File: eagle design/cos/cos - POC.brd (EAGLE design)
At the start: 35 x 63 mm, 105 parts, among them IC1 SQJ952EP-T1_GE3, IC10 PBRC8.00GR50X000, IC12 LM74670QDGKRQ1, IC14 MCP73871-2CCI/ML, IC15 MCP23S08-E/ML, IC16 LDK320M50R, IC17 MCP2515, IC18 LM74670QDGKRQ1, IC19 MCP2561-2, IC2 SQJ952EP-T1_GE3, IC20 AD5160BRJZ5-R2, IC21 MP3221GJ-P, IC22 SQJ952EP-T1_GE3, IC23 LM74670QDGKRQ1, IC24 LM74670QDGKRQ1, IC3 TPS630702RNMT, IC4 LM74670QDGKRQ1, IC5 SQJ952EP-T1_GE3, IC6 FDMQ8403, IC7 LMP92064SD/NOPB, IC8 ATTINY4313-MMH, IC9 LM74670QDGKRQ1

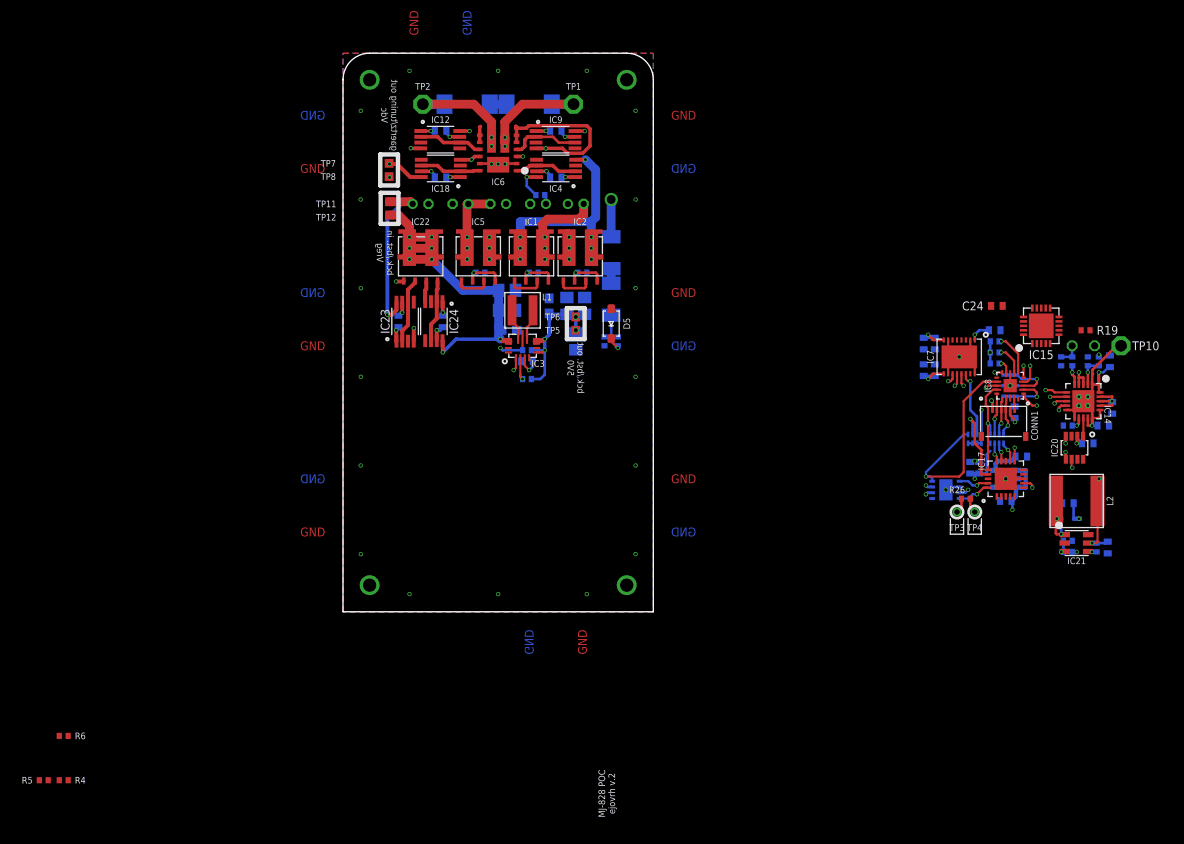
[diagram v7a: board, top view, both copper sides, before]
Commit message: - further work on schematic and routing: major reroute of parts, board size final
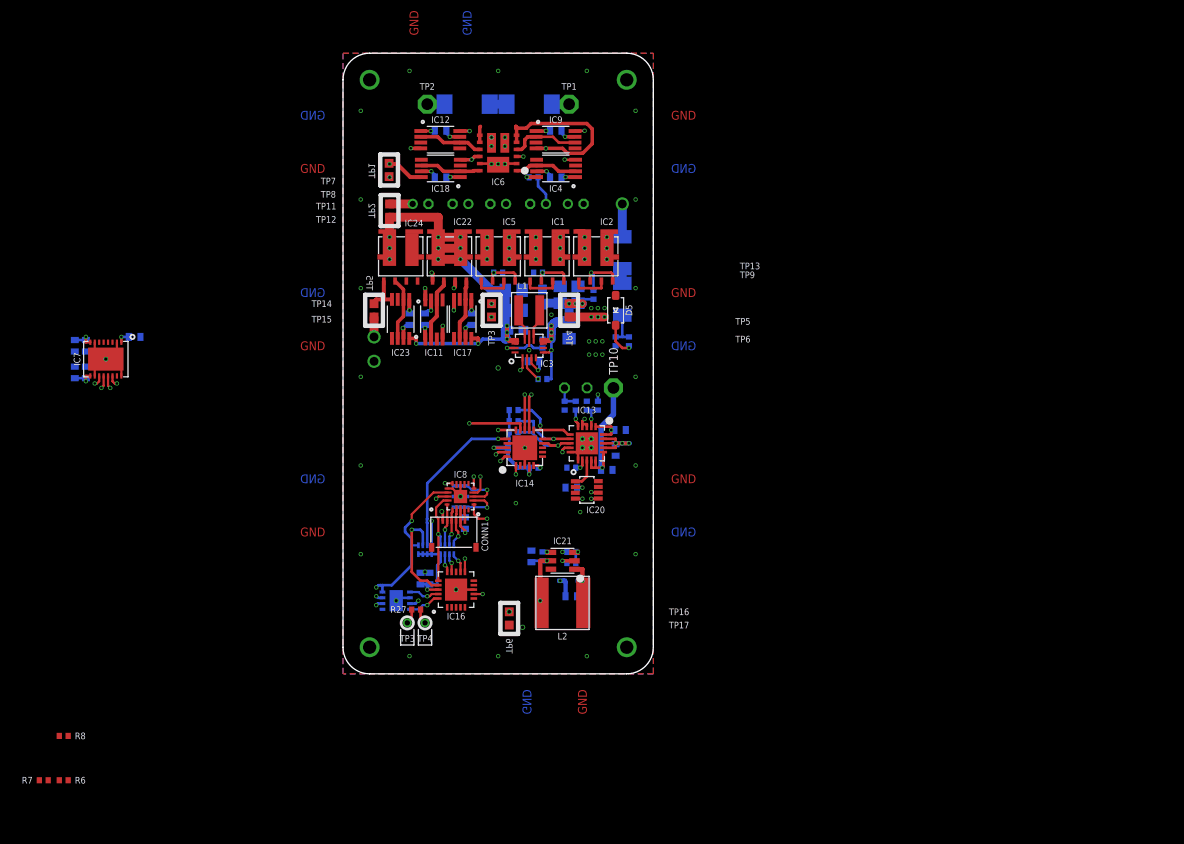
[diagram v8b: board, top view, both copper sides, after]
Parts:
- removed C28: 1μF, rcl:C0402
- removed C30: 4.7μF, rcl:C0402
- removed IC15: MCP23S08-E/ML, MCP23S08 - 8-Bit IO Expander with Serial Interface:QFN20
- added C22: 0.1μF, rcl:C0402
- added IC11: LM74670QDGKRQ1, LM74670 - Smart Diode Rectifier Controller:VSSOP-8
- added IC13: MCP73871-2CCI/ML, MCP73871 - Powerpath and Charge Controller:QFN50P400X400X100-21N
- added TP13, TP14, TP15, TP16, TP17, TP9: PTR1TP10SQ, testpad:TP10SQ
- C29: value 1μF -> 0.1μF
- C31: value 0.1μF -> 4.7μF
- C33: value 10μF -> 0.1μF
- C34: value 0.1μF -> 10μF
- C35: value 22μF -> 0.1μF
- C36: value 0.1μF -> 22μF
- D1, D2: value CZRB5353B-HF -> 1N4148W-7-F; device diode:DO214AA -> diode:SOD-123_MINI-SMA
- D3, D4: value 1N4148W-7-F -> CZRB5353B-HF; device diode:SOD-123_MINI-SMA -> diode:DO214AA
- IC14: value MCP73871-2CCI/ML -> MCP23S08-E/ML; device MCP73871 - Powerpath and Charge Controller:QFN50P400X400X100-21N -> MCP23S08 - 8-Bit IO Expander with Serial Interface:QFN20
- IC16: value LDK320M50R -> MCP2515; device LDK320 5V LDO:SOT-23-5L -> MCP2515-I-ML - Standalonce CAN Controller with SPI Interface:QFN20
- IC17: value MCP2515 -> LM74670QDGKRQ1; device MCP2515-I-ML - Standalonce CAN Controller with SPI Interface:QFN20 -> LM74670 - Smart Diode Rectifier Controller:VSSOP-8
- IC24: value LM74670QDGKRQ1 -> SQJ952EP-T1_GE3; device LM74670 - Smart Diode Rectifier Controller:VSSOP-8 -> SQJ952EP-T1_GE3 - Dual N-Fet:SO-8L
- R10: value 47k -> 337k
- R11: value 47k -> 110k
- R13, R3: value 10k -> 47k
- R14: value 100k -> 47k
- R15: value 1k -> 10k
- R16: value 270k -> 100k
- R17: value 741X083331JP / 330Ω -> 100k; device 741X083331JP Resistor Array:0402 -> rcl:R0402
- R18: value 741X083103JP / 10kΩ -> 1k; device 741X083331JP Resistor Array:0402 -> rcl:R0402
- R19: value 10k -> 270k
- R2: value 47k -> 22k
- R20: value thermistor NTC 10k -> 741X083331JP / 330Ω; device rcl:V526-0 -> 741X083331JP Resistor Array:0402
- R21: value 22k -> 741X083103JP / 10kΩ; device rcl:R0402 -> 741X083331JP Resistor Array:0402
- R22, R5: value 100k -> 10k
- R23: value 100k -> thermistor NTC 10k; device rcl:R0402 -> rcl:V526-0
- R24: value 653k -> 100k
- R25: value 100k -> 653k
- R26: value 120 -> 100k
- R27: value 100k -> 120
- R7: value 10k -> 100k
- R8: value 337k -> 100k
- R9: value 110k -> 10k
- moved R8 124.2 mm to (49.5, -15.0), flipped to the top, turned to 0 degrees
- moved C12 97.0 mm to (57.5, 30.0)
- moved IC7 96.3 mm to (54.2, 27.5)
- moved C14 95.8 mm to (50.8, 29.0)
- moved C15 95.8 mm to (52.0, 29.0)
- moved C16 95.8 mm to (50.8, 26.0)
- moved C17 95.8 mm to (52.0, 26.0)
- moved R5 82.7 mm to (109.2, 34.8), flipped to the bottom, turned to 270 degrees
- moved R4 80.7 mm to (113.2, 29.5), flipped to the bottom, turned to 270 degrees
- moved C33 77.6 mm to (89.8, 2.75), turned to 90 degrees
- moved R7 75.5 mm to (47.2, -20.0), flipped to the top
- moved R20 75.3 mm to (92.8, 6.00), turned to 270 degrees
- moved C32 68.1 mm to (92.0, 48.0), turned to 0 degrees
- moved R9 67.2 mm to (98.5, 37.2), turned to 0 degrees
- moved C34 64.0 mm to (102.2, 5.25), turned to 90 degrees
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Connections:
- removed net 5V0_LDO: C19.1, C24.1, C27.1, C29.2, C32.1, CONN1.5, IC15.18_VCC, IC16.OUT, IC17.VDD, IC19.VDD, IC8.18, R17.8, R18.1, R18.3, R18.5, R18.7, R19.2, R3.2
- removed net 5V9_LDO: IC15.4_!RESET!
- removed net 6V0: C28.1, C35.1, D6.C, IC16.EN, IC16.IN, R24.2
- removed net MCP23S08_GP0: IC15.9_GP0
- removed net MCP23S08_GP1: IC15.10_GP1
- removed net MCP23S08_GP2: IC15.11_GP2
- removed net MCP23S08_GP3: IC15.12_GP3
- removed net MCP23S08_GP4: IC15.13_GP4
- removed net MCP23S08_GP5: IC15.14_GP5
- removed net MCP23S08_GP6: IC15.15_GP6
- removed net V_LI-ION_BATTERY: C21.1, IC14.14_VBAT1, IC14.15_VBAT2, IC14.16_BAT_SENSE, IC22.S2, IC24.ANODE, TP10.TP
- new net 6V0_TP-IN: C36.1, D6.C, R25.2, TP16.TP
- new net 6V0_TP-OUT: TP17.TP
- new net D_VLIION_VCAPH1: C37.2, IC23.VCAPH
- new net D_VLIION_VCAPL1: C37.1, IC23.VCAPL
- new net GATE_SOLAR-CELL: IC23.GATE_DRIVE, IC23.GATE_PULLD, IC24.G1
- new net N$2: IC8.6
- new net N$6: IC8.7
- new net N$7: IC8.9
- new net SOLAR-CELL_TP-IN: TP15.TP
- new net SOLAR-CELL_TP-OUT: IC23.ANODE, IC24.S1, TP14.TP
- new net V_LI-ION_BATTERY-CELL: C21.1, IC13.14_VBAT1, IC13.15_VBAT2, IC13.16_BAT_SENSE, TP10.TP
- new net V_LI-ION_TP-OUT: IC17.ANODE, TP9.TP
- net 5V0_TP-IN: now also R15.2, R17.2, R5.2; no longer R13.2, R27.2
- net 5V0_TP-OUT: now also C19.1, C24.1, C27.1, C33.1, C35.1, CONN1.5, IC13.17_CE, IC13.18_IN1, IC13.19_IN2, IC13.3_SEL, IC13.4_PROG2, IC13.9_!TE!, IC14.18_VCC, IC14.4_!RESET!, IC16.VDD, IC19.VDD, IC8.18, R13.2, R14.2, R20.8, R21.1, R21.3, R21.5, R21.7, R22.2; no longer C34.1, IC14.17_CE, IC14.18_IN1, IC14.19_IN2, IC14.3_SEL, IC14.4_PROG2, IC14.9_!TE!, R11.2, R8.2
- net AD5160_CS: now also IC14.15_GP6, R21.8; no longer IC8.1, R18.8
- net CANH: now also R27.2; no longer R26.2
- net CANL: now also R27.1; no longer R26.1
- net CLOCKOUT: now also IC16.OSC1; no longer IC17.OSC1
- net COMP_IN: now also R4.2; no longer R22.2
- net D4_VCAPH: now also C32.2; no longer C31.2
- net D4_VCAPL: now also C32.1; no longer C31.1
- net DYNAMO_1: now also D4.A; no longer D2.A
- net DYNAMO_2_AFTER_SW: now also D1.A, IC4.ANODE, IC6.3_S1/D2, IC6.S1/D2, IC9.CATHODE; no longer D3.A, IC5.D2_1, IC5.D2_2, IC5.D2_3
- net DYNAMO_2_BEFORE_SW: now also D3.A, IC5.D2_1, IC5.D2_2, IC5.D2_3; no longer D1.A, IC4.ANODE, IC6.3_S1/D2, IC6.S1/D2, IC9.CATHODE
- net D_SMOOTH_VCAP: now also C22.1, IC11.VCAPL; no longer C36.1, IC23.VCAPL
- net D_SMOOTH_VCAPH: now also C22.2, IC11.VCAPH; no longer C36.2, IC23.VCAPH
- net D_VLIION_VCAPH: now also C29.2, IC17.VCAPH; no longer C37.2, IC24.VCAPH
- net D_VLIION_VCAPL: now also C29.1, IC17.VCAPL; no longer C37.1, IC24.VCAPL
- net EN: now also IC3.14-EN, R15.1; no longer R13.1
- net EN2: now also R24.1; no longer R23.1
- net FB: now also R25.1, R26.2; no longer R24.1, R25.2
- net GATE_DELON: now also IC14.14_GP5, R9.2; no longer R7.2
- net GATE_DIODE_SMOOTH: now also IC11.GATE_DRIVE, IC11.GATE_PULLD; no longer IC23.GATE_DRIVE, IC23.GATE_PULLD
- net GATE_DIODE_V_LIION: now also IC17.GATE_DRIVE, IC17.GATE_PULLD; no longer IC24.GATE_DRIVE, IC24.GATE_PULLD
- net GATE_GRAETZ: now also IC14.12_GP3, R5.1; no longer R3.1
- net GATE_TUNING-CAP: now also IC14.13_GP4
- net GND: now also C31.1, C36.2, IC13.10_GND1, IC13.11_GND2, IC13.GND2, IC13.GND3, IC13.GND4, IC13.GND5, IC13.GND6, IC14.17_GND, IC14.2_A1, IC14.3_A0, IC14.GND, IC16.GND6, R11.1, R19.1, R2.1, R23.1, R26.1; no longer C28.2, C29.1, C30.1, C32.2, IC14.10_GND1, IC14.11_GND2, IC14.GND2, IC14.GND3, IC14.GND4, IC14.GND5, IC14.GND6, IC15.17_GND, IC15.2_A1, IC15.3_A0, IC15.GND, IC17.GND, IC17.GND6, R14.1, R20.1, R21.1, R25.1, R7.1
- net ICSP_DI/MISO: now also R20.5; no longer R17.5
- net ICSP_DO/MOSI: now also R20.3; no longer R17.3
- net ICSP_SCK: now also R20.1; no longer R17.1
- net INT_MCP23S08: now also IC14.7_INT; no longer IC15.7_INT
- net INT_MCP2515: now also IC16.!INT!; no longer IC17.!INT!
- net LMP92064SD_CS: now also IC14.16_GP7, R21.6; no longer IC15.16_GP7, R18.6
- net MCP73871_PG_PIN: now also IC13.!6_PG!, IC14.11_GP2, R12.1; no longer IC14.!6_PG!, IC8.9, R10.1
- net MCP73871_STAT1/!LBO!_PIN: now also IC13.8_STAT1/!LBO!, IC14.9_GP0, R13.1; no longer IC14.8_STAT1/!LBO!, IC8.6, R11.1
- net MCP73871_STAT2_PIN: now also IC13.7_STAT2, IC14.10_GP1, R14.1; no longer IC14.7_STAT2, IC8.7, R12.1
- net N$14: now also R6.1, R7.2; no longer R4.1, R5.2
- net N$3: now also D1.C, D2.A; no longer D3.C, D4.A
- net N$4: now also D2.C, R2.2, R4.1; no longer D4.C, R21.2, R22.1
- net N$8: now also R18.2, R19.2, R23.2; no longer R15.2, R16.2, R20.2
- net PG: now also R17.1; no longer R27.1
- net PROG1: now also IC13.13_PROG1; no longer IC14.13_PROG1
- net PROG3: now also IC13.12_PROG3, R16.2; no longer IC14.12_PROG3, R14.2
- net RESET: now also IC16.!RESET!, R21.4; no longer IC17.!RESET!, R18.4
- net RXCAN: now also IC16.RXCAN; no longer IC17.RXCAN
- net SPI_MISO: now also IC14.20_MISO, IC16.SO, R20.6; no longer IC15.20_MISO, IC17.SO, R17.6
- net SPI_MOSI: now also IC14.1_MOSI, IC16.SI, R20.4; no longer IC15.1_MOSI, IC17.SI, R17.4
- net SPI_SCK: now also IC14.19_SCK, IC16.SCK, R20.2; no longer IC15.19_SCK, IC17.SCK, R17.2
- net SPI_SS_MCP23S08: now also IC14.5_!CS!, IC8.1, R22.1; no longer IC15.5_!CS!, R19.1
- net SPI_SS_MCP2515: now also IC16.!CS!, R20.7; no longer IC17.!CS!, R17.7
- net STBY: now also R21.2; no longer R18.2
- net THERM: now also IC13.5_THERM, R18.1; no longer IC14.5_THERM, R15.1
- net TUNIN_CAP2_BIAS: now also R3.1; no longer R2.1
- net TXCAN: now also IC16.TXCAN; no longer IC17.TXCAN
- net VPCC: now also IC13.2_VPCC, R10.1, R11.2; no longer IC14.2_VPCC, R8.1, R9.2
- net V_DC_TP-IN: now also R3.2; no longer R2.2
- net V_DC_TP-OUT: now also IC11.ANODE; no longer IC23.ANODE
- net V_LI-ION_OUT: now also C31.2, C34.1, IC13.1_OUT1, IC13.20_OUT2, IC22.S2, R24.2, TP13.TP; no longer C30.2, C33.1, IC14.1_OUT1, IC14.20_OUT2, R23.2
- net V_REGULATED_TP-IN: now also IC11.CATHODE; no longer IC23.CATHODE
- net V_REGULATED_TP-OUT: now also IC17.CATHODE, IC23.CATHODE, IC24.D1_1, IC24.D1_2, IC24.D1_3; no longer IC24.CATHODE, IC3.14-EN
- net ZENER_COMMON: now also D3.C, D4.C; no longer D1.C, D2.C
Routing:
- net V_LI-ION_OUT: track 28.1 -> 87.8 mm, vias 3 -> 6
- net 5V0_TP-OUT: track 21.3 -> 51.9 mm, vias 8 -> 17
- net COMP_IN: track 2.49 -> 32.4 mm
- net 6V0: track 21.6 -> 0.00 mm, vias 3 -> 0
- net V_REGULATED_TP-OUT: track 52.4 -> 71.0 mm, vias 8 -> 14
- net V_LI-ION_BATTERY: track 17.8 -> 0.00 mm, vias 1 -> 0
- net GATE_DELON: track 11.4 -> 28.9 mm, vias 1 -> 2
- net V_LI-ION_BATTERY-CELL: track 0.00 -> 16.0 mm, vias 0 -> 1
- net GATE_GRAETZ: track 11.7 -> 27.3 mm, vias 1 -> 2
- net 6V0_TP-IN: track 0.00 -> 15.3 mm, vias 0 -> 3
- net SPI_SS_MCP23S08: track 0.00 -> 13.9 mm, vias 0 -> 2
- net SPI_SCK: track 22.3 -> 36.1 mm, vias 3 -> 5
- net 5V0_LDO: track 12.5 -> 0.00 mm, vias 3 -> 0
- net AD5160_CS: track 21.1 -> 33.4 mm
- net LMP92064SD_CS: track 7.58 -> 19.4 mm, vias 1 -> 2
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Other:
- board size 35 x 63 mm -> 35 x 70 mm
- board text added: "TP1"
- board text added: "TP2"
- board text added: "TP3"
- board text added: "TP4"
- board text added: "TP5"
- board text added: "TP6"
- board text added: "Čos POC ejovrh rev.1"
- board text removed: "MJ-828 POC ejovrh v.2"
- board text removed: "bck./bst. in Vreg"
- board text removed: "bck./bst. out 5V0"
- board text removed: "gaertz/tuning out Vdc"
